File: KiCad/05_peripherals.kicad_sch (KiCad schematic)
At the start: 35 parts, among them IC501 VEML7700-TT, IC502 DS3231MZ+TRL, U502 DS18B20, U503 LM35-LP, U504 DHT11

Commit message: Production files prepare
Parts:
- IC501: Manufacturer Part Number VEML7700-TT -> VEML7700-TR
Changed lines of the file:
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@@
 			)
 		)
-		(property "Manufacturer Part Number" "VEML7700-TT"
+		(property "Manufacturer Part Number" "VEML7700-TR"
 			(at 160.02 64.77 0)
 			(effects

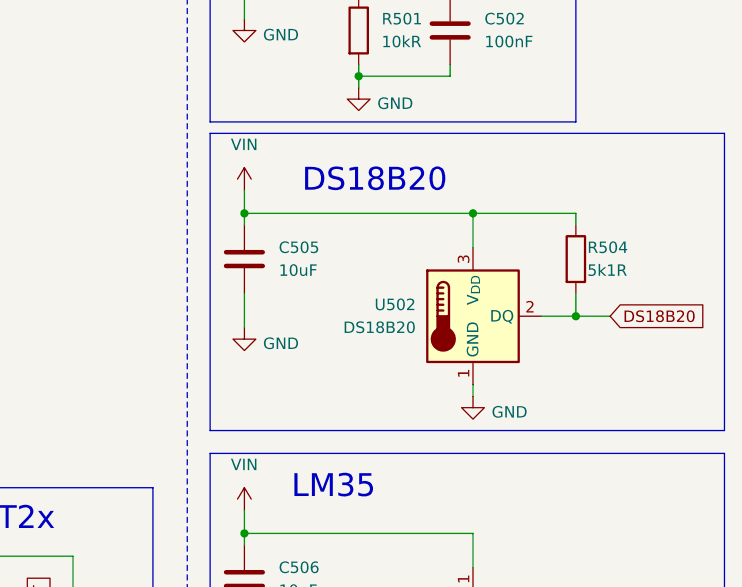
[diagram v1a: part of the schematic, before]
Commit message: Remove broken scheme parts
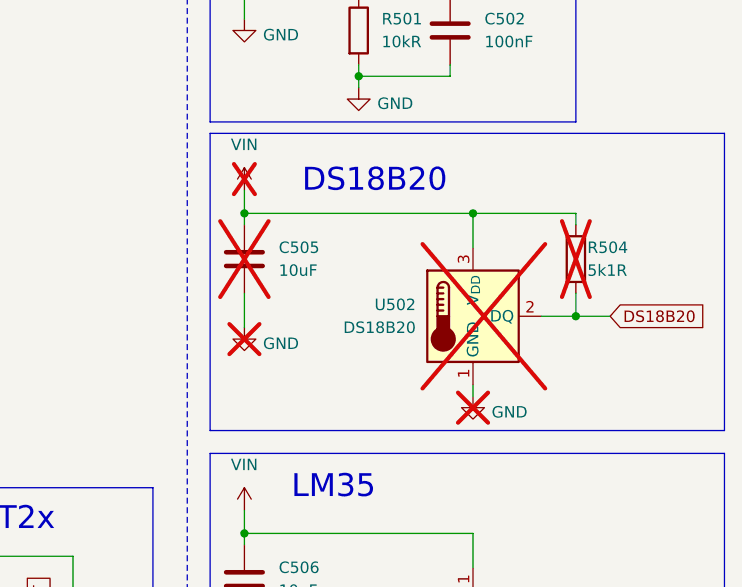
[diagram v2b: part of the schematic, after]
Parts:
- C501, C504, C506, C508, C510: Manufacturer Product Number CL21A106KOQNNNE -> (none)
- C502: Manufacturer Product Number CL10B104KB8NNNC -> (none)
- C505: Manufacturer Product Number CL21A106KOQNNNE -> (none); now not fitted
- IC501: Manufacturer_Name Vishay -> (none); Manufacturer_Part_Number VEML7700-TT -> (none); Mouser Part Number 78-VEML7700-TT -> (none); Mouser Price/Stock https://www.mouser.co.uk/ProductDetail/Vishay-Semiconductor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 -> (none)
- IC502: Manufacturer_Name Analog Devices -> (none); Manufacturer_Part_Number DS3231MZ+TRL -> (none); Mouser Part Number 700-DS3231MZ+TRL -> (none); Mouser Price/Stock https://www.mouser.co.uk/ProductDetail/Analog-Devices-Maxim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 -> (none)
- R501: Manufacturer Product Number 0805W8F1002T5E -> (none)
- R504, U502: now not fitted
- RLO501: Manufacturer Product Number GL5528(10-20) -> (none)
- U504: Manufacturer_Name Microchip -> (none); Manufacturer_Part_Number DHT11 -> (none)
